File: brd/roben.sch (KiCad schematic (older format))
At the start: 81 parts, among them J1 POWER IN, J10 1+, J11 1-, J12 2-, J13 2+, J2 +V, J3 GND, J4 +V, J5 GND, J6 A, U2 SN754410N, U3 Ardunano

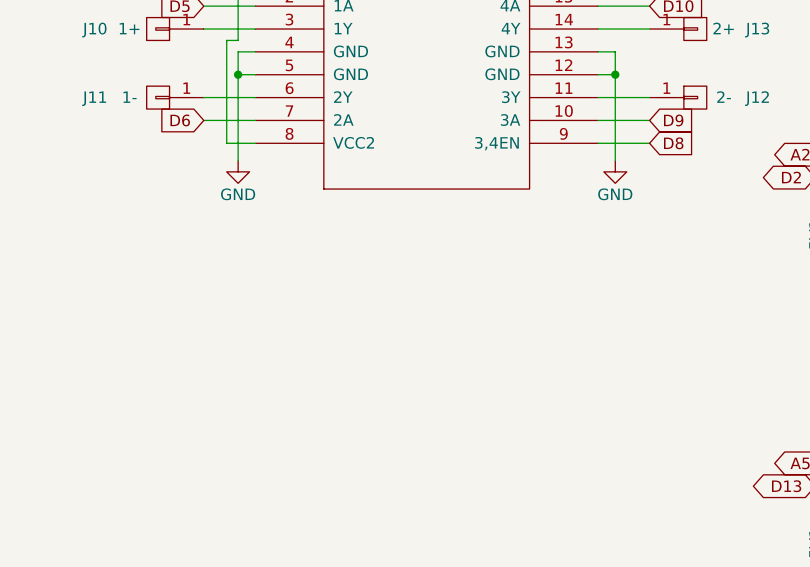
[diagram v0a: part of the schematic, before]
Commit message: chg: añadidos indicadores de salida en motores
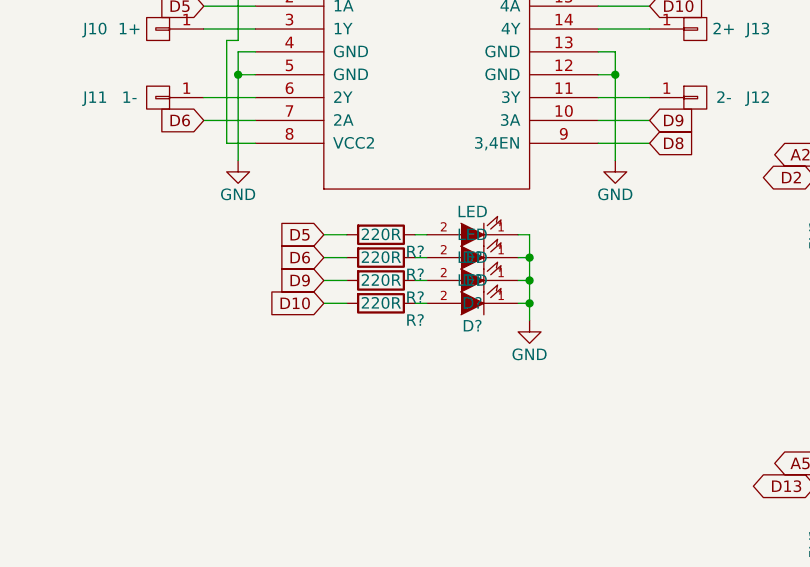
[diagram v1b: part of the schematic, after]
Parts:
- added D? (x4): LED, LEDs:LED-0805, symbol LED
- added R? (x4): 220R, Resistors_SMD:R_0805_HandSoldering, symbol R
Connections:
- net D10: now also R?.2
- net D5: now also R?.2
- net D6: now also R?.2
- net D9: now also R?.2
- net GND: now also D?.1 (K), D?.1 (K), D?.1 (K), D?.1 (K)
- new net: D?.2 (A), R?.1 (x4)
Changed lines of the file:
@@
 Wire Wire Line
 	3850 5000 3850 5075
+$Comp
+L LED D?
+U 1 1 56A6A54A
+P 6475 3425
+F 0 "D?" H 6475 3525 50  0000 C CNN
+F 1 "LED" H 6475 3325 50  0000 C CNN
+F 2 "LEDs:LED-0805" H 6475 3425 60  0001 C CNN
+F 3 "" H 6475 3425 60  0000 C CNN
+F 4 "720-LOR976-PS-1" H 6475 3425 60  0001 C CNN "Vendor"
+	1    6475 3425
+	-1   0    0    1
+$EndComp
+$Comp
+L R R?
+U 1 1 56A6A551
+P 6075 3425
+F 0 "R?" V 6150 3575 50  0000 C CNN
+F 1 "220R" V 6075 3425 50  0000 C CNN
+F 2 "Resistors_SMD:R_0805_HandSoldering" V 6005 3425 30  0001 C CNN
+F 3 "" H 6075 3425 30  0000 C CNN
+F 4 "71-CRCW0805-220-E3" V 6075 3425 60  0001 C CNN "Vendor"
+	1    6075 3425
+	0    1    1    0
+$EndComp
+$Comp
+L R R?
+U 1 1 56A6A558
+P 6075 3525
+F 0 "R?" V 6150 3675 50  0000 C CNN
+F 1 "220R" V 6075 3525 50  0000 C CNN
+F 2 "Resistors_SMD:R_0805_HandSoldering" V 6005 3525 30  0001 C CNN
+F 3 "" H 6075 3525 30  0000 C CNN
+F 4 "71-CRCW0805-220-E3" V 6075 3525 60  0001 C CNN "Vendor"
+	1    6075 3525
+	0    1    1    0
+$EndComp
+$Comp
+L LED D?
+U 1 1 56A6A55F
+P 6475 3525
+F 0 "D?" H 6475 3625 50  0000 C CNN
+F 1 "LED" H 6475 3425 50  0000 C CNN
+F 2 "LEDs:LED-0805" H 6475 3525 60  0001 C CNN
+F 3 "" H 6475 3525 60  0000 C CNN
+F 4 "720-LOR976-PS-1" H 6475 3525 60  0001 C CNN "Vendor"
+	1    6475 3525
+	-1   0    0    1
+$EndComp
+Wire Wire Line
+	6225 3425 6275 3425
+Wire Wire Line
+	6225 3525 6275 3525
+Wire Wire Line
+	6725 3425 6725 3800
+Wire Wire Line
+	6725 3425 6675 3425
+Wire Wire Line
+	6675 3525 6725 3525
+Connection ~ 6725 3525
+$Comp
+L LED D?
+U 1 1 56A6ADBC
+P 6475 3625
+F 0 "D?" H 6475 3725 50  0000 C CNN
+F 1 "LED" H 6475 3525 50  0000 C CNN
+F 2 "LEDs:LED-0805" H 6475 3625 60  0001 C CNN
+F 3 "" H 6475 3625 60  0000 C CNN
+F 4 "720-LOR976-PS-1" H 6475 3625 60  0001 C CNN "Vendor"
+	1    6475 3625
+	-1   0    0    1
+$EndComp
+$Comp
+L R R?
+U 1 1 56A6ADC3
+P 6075 3625
+F 0 "R?" V 6150 3775 50  0000 C CNN
+F 1 "220R" V 6075 3625 50  0000 C CNN
+F 2 "Resistors_SMD:R_0805_HandSoldering" V 6005 3625 30  0001 C CNN
+F 3 "" H 6075 3625 30  0000 C CNN
+F 4 "71-CRCW0805-220-E3" V 6075 3625 60  0001 C CNN "Vendor"
+	1    6075 3625
+	0    1    1    0
+$EndComp
+$Comp
+L R R?
+U 1 1 56A6ADCA
+P 6075 3725
+F 0 "R?" V 6150 3875 50  0000 C CNN
+F 1 "220R" V 6075 3725 50  0000 C CNN
+F 2 "Resistors_SMD:R_0805_HandSoldering" V 6005 3725 30  0001 C CNN
+F 3 "" H 6075 3725 30  0000 C CNN
+F 4 "71-CRCW0805-220-E3" V 6075 3725 60  0001 C CNN "Vendor"
+	1    6075 3725
+	0    1    1    0
+$EndComp
+$Comp
+L LED D?
+U 1 1 56A6ADD1
+P 6475 3725
+F 0 "D?" H 6475 3825 50  0000 C CNN
+F 1 "LED" H 6475 3625 50  0000 C CNN
+F 2 "LEDs:LED-0805" H 6475 3725 60  0001 C CNN
+F 3 "" H 6475 3725 60  0000 C CNN
+F 4 "720-LOR976-PS-1" H 6475 3725 60  0001 C CNN "Vendor"
+	1    6475 3725
+	-1   0    0    1
+$EndComp
+$Comp
+L GND #PWR?
+U 1 1 56A6ADD7
+P 6725 3800
+F 0 "#PWR?" H 6725 3550 50  0001 C CNN
+F 1 "GND" H 6725 3650 50  0000 C CNN
+F 2 "" H 6725 3800 60  0000 C CNN
+F 3 "" H 6725 3800 60  0000 C CNN
+	1    6725 3800
+	1    0    0    -1
+$EndComp
+Wire Wire Line
+	6225 3625 6275 3625
+Wire Wire Line
+	6225 3725 6275 3725
+Wire Wire Line
+	6725 3625 6675 3625
+Wire Wire Line
+	6675 3725 6725 3725
+Connection ~ 6725 3725
+Connection ~ 6725 3625
+Text GLabel 5825 3425 0    50   Input ~ 0
+D5
+Text GLabel 5825 3525 0    50   Input ~ 0
+D6
+Text GLabel 5825 3625 0    50   Input ~ 0
+D9
+Text GLabel 5825 3725 0    50   Input ~ 0
+D10
+Wire Wire Line
+	5825 3725 5925 3725
+Wire Wire Line
+	5925 3625 5825 3625
+Wire Wire Line
+	5825 3525 5925 3525
+Wire Wire Line
+	5925 3425 5825 3425
 $EndSCHEMATC

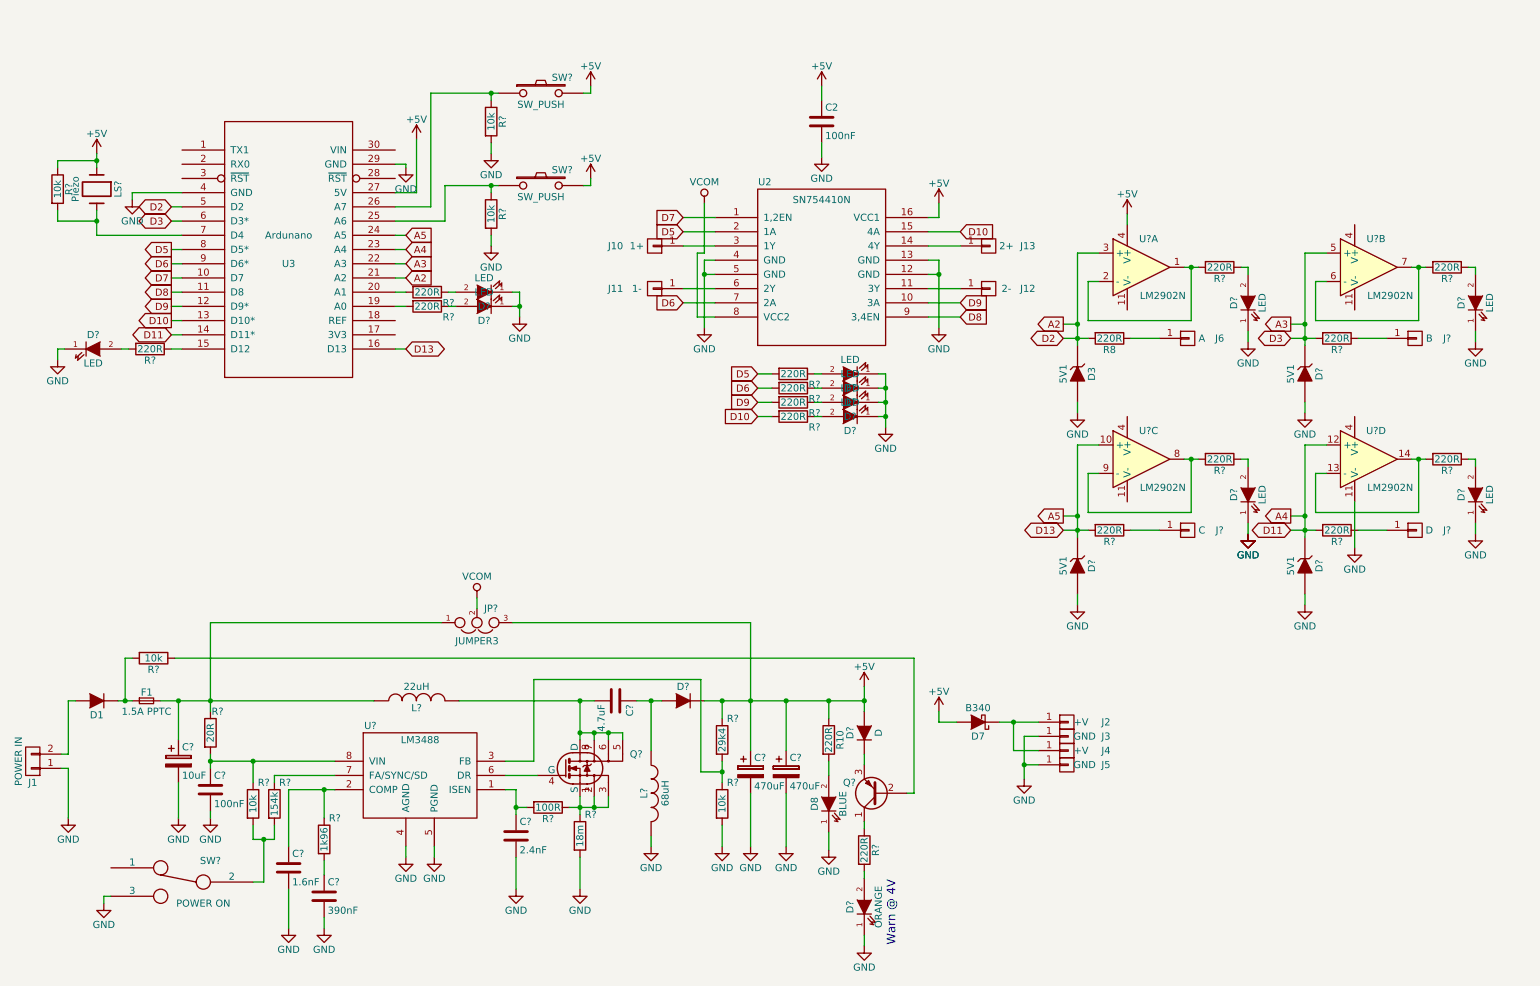
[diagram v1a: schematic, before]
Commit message: chg: añadida comunicacion bluetooth
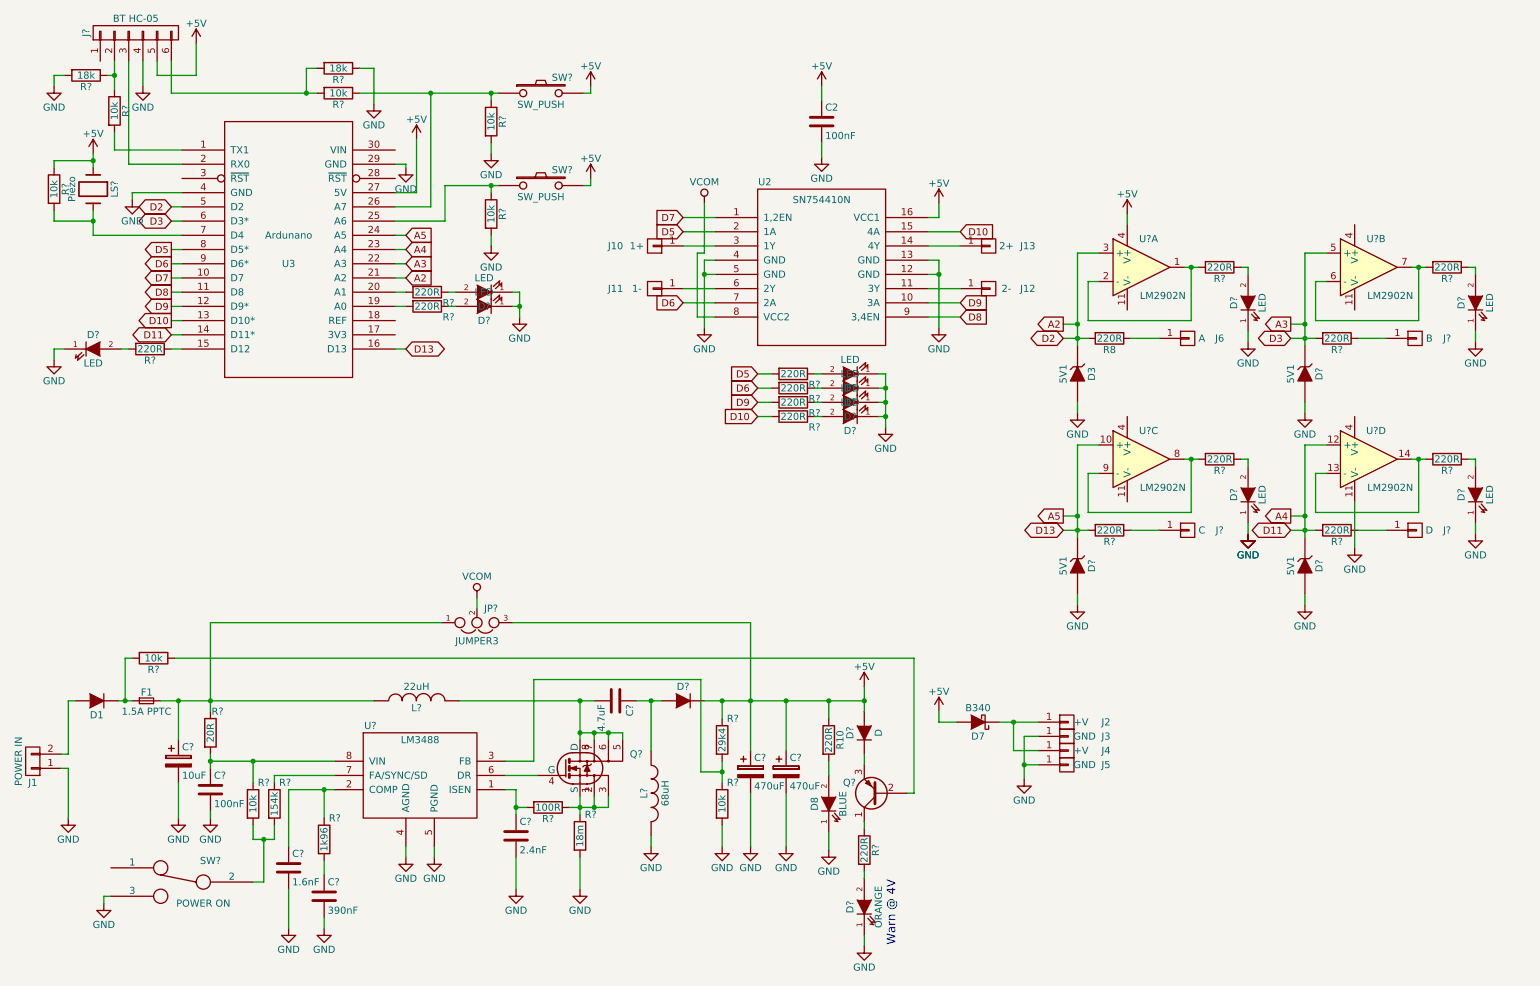
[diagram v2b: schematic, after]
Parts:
- added J?: BT HC-05, symbol CONN_01X06
- added R? (x2): 10k, symbol R
- added R? (x2): 18k, symbol R
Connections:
- net +5V: now also J?.5 (P5)
- net GND: now also J?.4 (P4), R?.1, R?.2
- net at U3.1 (TX1): now also R?.2
- net at U3.2 (RX0): now also J?.3 (P3)
- net at R?.1, SW?.1, U3.26 (A7): now also R?.1
- new net: J?.2 (P2), R?.1, R?.1
- new net: J?.6 (P6), R?.2, R?.2
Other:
- moved on the sheet: LS?, R?

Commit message: chg: anotados componentes en esquematico
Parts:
- removed D1: B340, Diodes_SMD:Diode-SMC_Handsoldering, symbol D
- added C10: 100nF, Capacitors_SMD:C_0805_HandSoldering, symbol C
- added D2: B340, Diodes_SMD:Diode-SMC_Handsoldering, symbol D_Schottky
- C9: renamed from C2; Vendor 843-0805J0500104KJT -> C0805C104K5RACTU
- D1: renamed from D?; value LED -> RED; Vendor 720-LOR976-PS-1 -> LS Q976-NR-1
- D10, D16, D17, D20, D21, D7, D8, D9: renamed from D?; value LED -> ORANGE; Vendor 720-LOR976-PS-1 -> LO R976-PS-1
- D13: renamed from D7; Vendor 621-B340-F -> B340-F
- D14: renamed from D3; Vendor 821-BZT52B5V1 -> BZT52B5V1
- D15, D18, D19: renamed from D?; Vendor 821-BZT52B5V1 -> BZT52B5V1
- D3: renamed from D?; value LED -> YELLOW; Vendor 720-LOR976-PS-1 -> LY R976-PS-36
- D4: renamed from D?; value LED -> GREEN; Vendor 720-LOR976-PS-1 -> LG R971-KN-1
- J2: renamed from J?; Vendor (none) -> 61303211821
- JP1: renamed from JP?; value JUMPER3 -> VSEL; Vendor (none) -> M20-8771646
- LS1: renamed from LS?; value Piezo -> AT-1224-TWT-5V-2-R; Vendor (none) -> AT-1224-TWT-5V-2-R
- R1, R11, R14, R15, R3: renamed from R?; Vendor (none) -> ERJ-6ENF1002V
- R10, R2: renamed from R?; Vendor (none) -> ERJ-6ENF1802V
- R12, R13, R20, R21, R22, R23, R27, R28, R29, R30, R31, R32, R33, R4: renamed from R?; Vendor 71-CRCW0805-220-E3 -> ERJ-6GEYJ221V
- R26: renamed from R8; Vendor 71-CRCW0805-220-E3 -> ERJ-6GEYJ221V
- SW2, SW3: renamed from SW?; Vendor (none) -> FSM18JH
- U1: renamed from U3; Vendor 992-ARD-NANO30 -> A000005 / 1-2199300-2
- U3: renamed from U2; Vendor 595-SN754410NE -> SN754410NE / 1-2199298-4
- U4: renamed from U?; Vendor (none) -> LM2902DT
- gave numbers to parts that had none: 30
- renumbered D8 to D6, J5 to J10, J6 to J11, J10 to J3, J11 to J4, J13 to J5, J12 to J6, J2 to J7, J3 to J8, J4 to J9, R10 to R24
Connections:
- net +5V: now also C10.1
- net A3: now also U4.10 (+); no longer U4.5 (+)
- net A5: now also U4.5 (+); no longer U4.10 (+)
- net GND: now also C10.2
- net at J1.2 (P2): now also D2.2 (A)
- net at F1.1, R5.2: now also D2.1 (K)
- new net: R32.2, U4.8, U4.9 (-)
- new net: R29.2, U4.6 (-), U4.7
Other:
- moved on the sheet: D10, D7, D8, D9, R20, R21, R22, R23
